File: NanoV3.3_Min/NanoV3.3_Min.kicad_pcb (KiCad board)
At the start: 2 copper layers, 43.2 x 17.8 mm, 28 parts, among them IC1 FT232RL, IC3 328P-MUR, J1 Conn_1x15, J2 Conn_1x15, J3 Conn_Mini_USB, Y1 16MHz

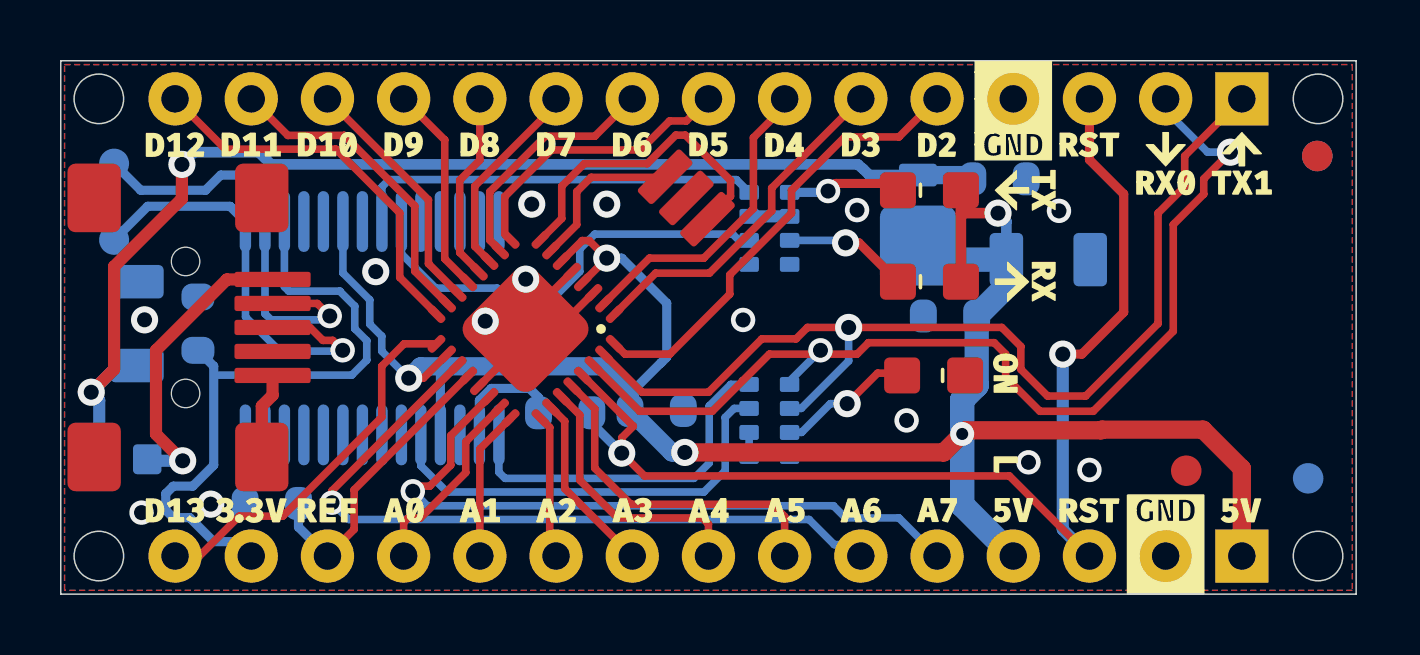
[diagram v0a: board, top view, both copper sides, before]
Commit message: finalized first iteration of nano minima
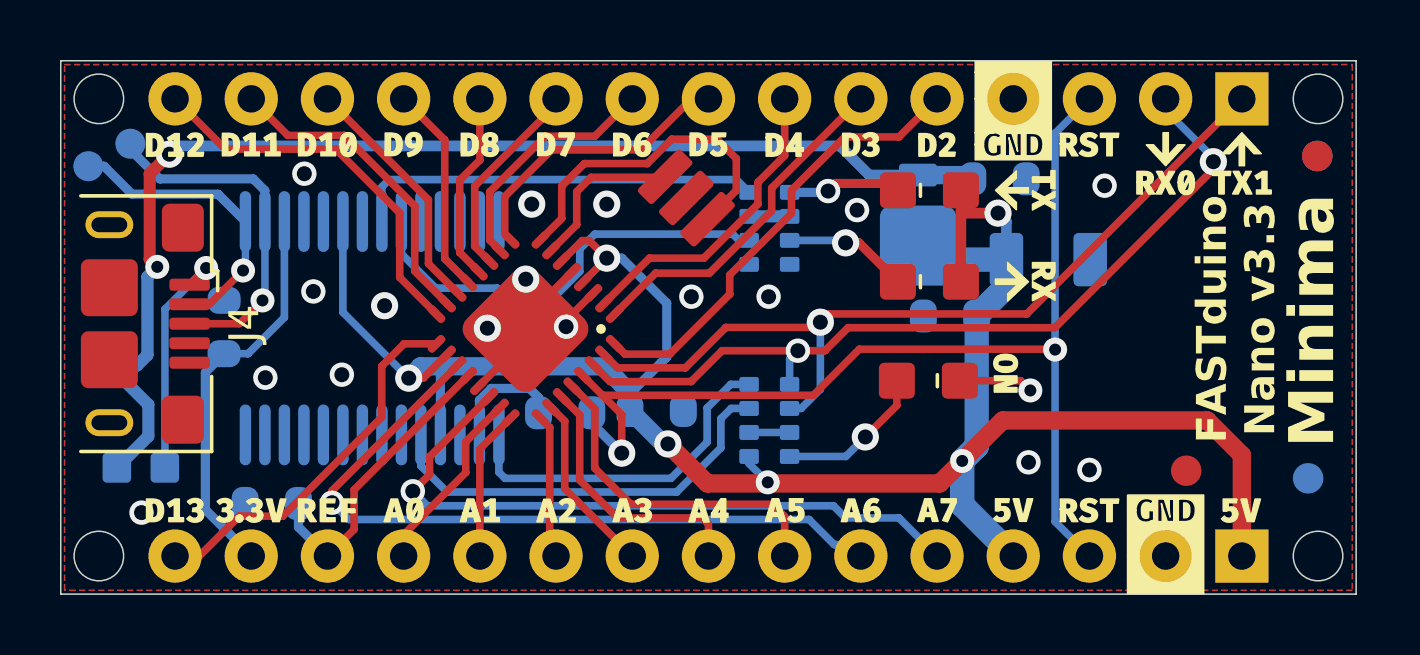
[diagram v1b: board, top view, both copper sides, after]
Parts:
- removed J3: Conn_Mini_USB, NanoV3.3:USB_Mini-B_Lumberg_2486_01_Horizontal
- added J4: USB_B_Micro, Connector_USB:USB_Micro-B_Amphenol_10118193-0001LF_Horizontal, F.Cu at (127.3, 101.5)
- moved D+0 2.60 mm to (126.7, 96.2)
- moved C2 0.95 mm to (127.3, 102.8)
- moved C6 0.88 mm to (131.2, 101.6)
- moved D-0 0.86 mm to (128.1, 95.5)
- moved F1 0.65 mm to (128.4, 106.3)
- moved PWR1 0.25 mm to (154.7, 103.4)
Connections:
- PWR1 pad 1: Net-(RP1C-1) -> Net-(RP1D-1)
- RP1 pad 3: Net-(RP1C-1) -> COM
- RP1 pad 4: COM -> Net-(RP1D-1)
- RP1 pad 5: COM -> +5V
- RP1 pad 6: +5V -> COM
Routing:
- net 3V3: track 22.1 -> 13.3 mm
- net /D0/RX: track 35.0 -> 28.1 mm
- net /D1/TX: track 34.7 -> 28.7 mm
- net Net-(RP1D-1): track 0.00 -> 5.10 mm, vias 0 -> 1
- net Net-(D+0-P$1): track 14.5 -> 9.95 mm
- net Net-(RP1C-1): track 4.43 -> 0.00 mm, vias 2 -> 0
- net Net-(D-0-P$1): track 14.5 -> 11.7 mm
- net /RESET: track 39.5 -> 36.8 mm
- net Net-(J4-VBUS): track 10.0 -> 8.01 mm
- net +5V: track 73.7 -> 75.4 mm, vias 5 -> 6
- net COM: track 12.1 -> 13.1 mm, vias 13 -> 18
- net Net-(IC3-PB7(XTAL2/TOSC2)): track 10.7 -> 11.2 mm
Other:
- board text added: "FASTduino Nano v3.3"
- board text added: "Minima"

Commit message: added bom start
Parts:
- removed FD1, FD2, FD3, FD4: DNP, NanoV3.3:Fiducial_1mm_Mask1.5mm
- LEDG1: renamed from PWR1; value Green -> LTST-C171GKT
- LEDO1: renamed from TX0; value Green -> LTST-C170KFKT
- LEDR1: renamed from RX0; value Red -> LTST-C171KRKT
- renumbered C7 to C2, C5 to C3, C3 to C4, C4 to C5, C2 to C6, C9 to C7, C6 to C8, D+0 to D+1, D-0 to D-1, IC3 to IC1, IC1 to IC2, J4 to J3
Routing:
- net COM: vias 18 -> 22
